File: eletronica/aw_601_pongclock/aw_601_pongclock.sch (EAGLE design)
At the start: 11 parts, among them IC1 MEGA8-P, IC2 4515N, IC3 4515N, IC4 4094N, IC5 4094N, IC6 4094N, IC7 4094N

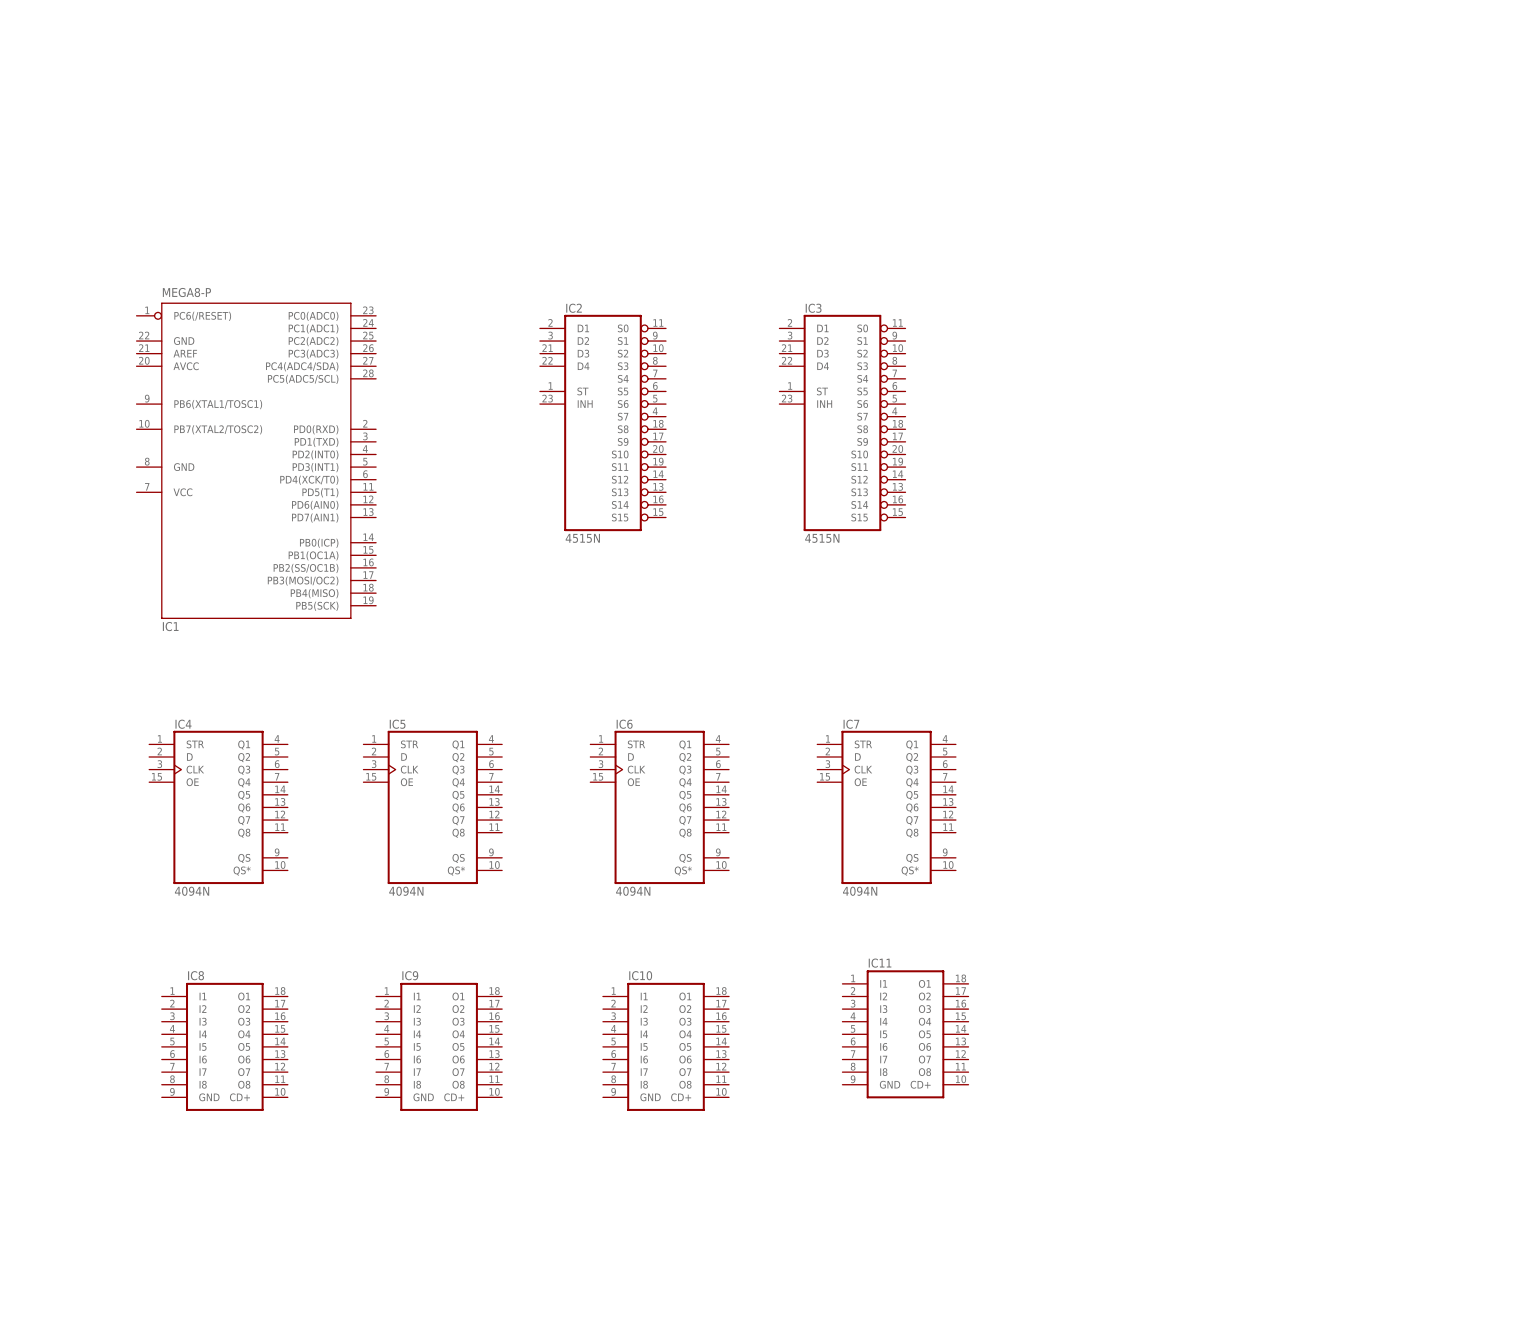
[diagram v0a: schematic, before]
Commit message: 
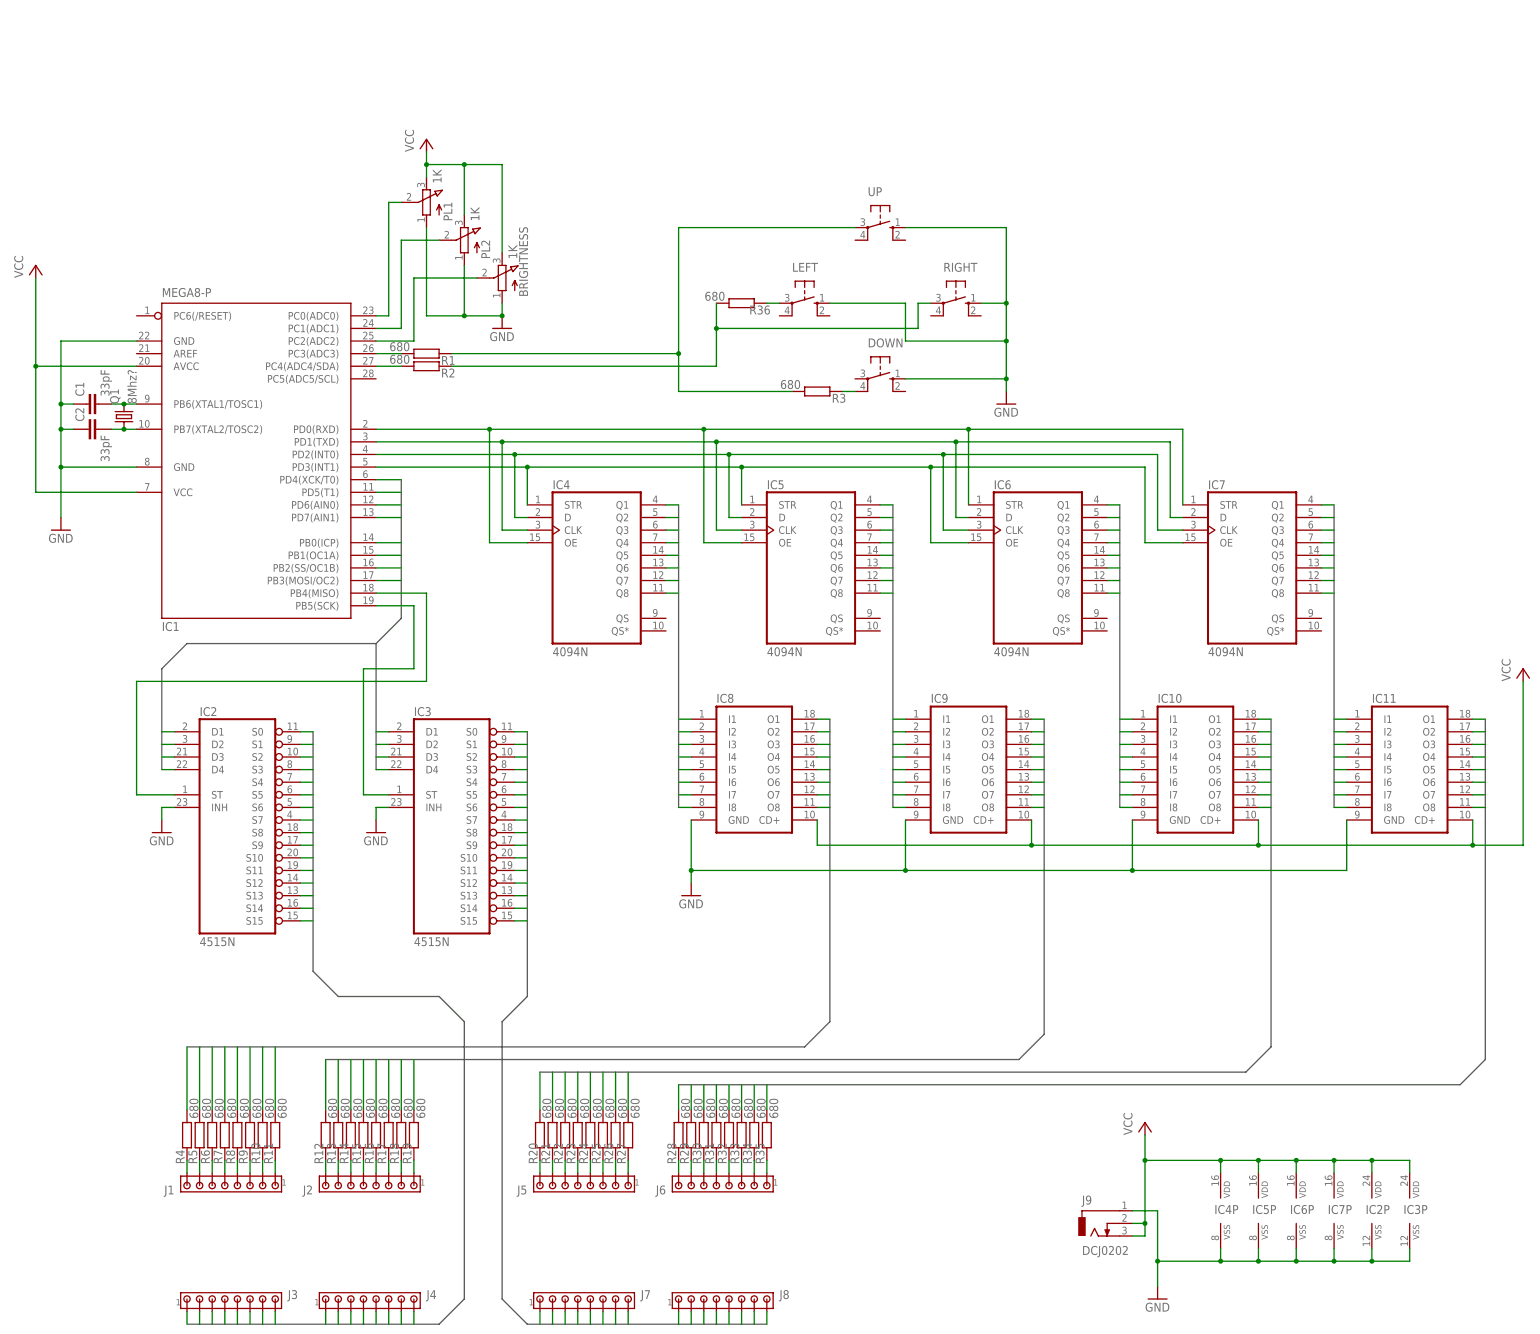
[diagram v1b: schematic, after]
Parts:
- added BRIGHTNESS, PL1, PL2: 1K, pot:3RP/1610N
- added C1, C2: 33pF, rcl:C-EU025-025X050
- added DOWN, LEFT, RIGHT, UP: (no value), switch-omron:40/XX
- added J1, J2, J3, J4, J5, J6, J7, J8: (no value), con-amp:MTA08-100
- added J9: DCJ0202, con-jack:DCJ0202
- added Q1: 8Mhz?, crystal:CRYSTALHC49U70
- added R1, R10, R11, R12, R13, R14, R15, R16, R17, R18, R19, R2, R20, R21, R22, R23, R24, R25, R26, R27, R28, R29, R3, R30, R31, R32, R33, R34, R35, R36, R4, R5, R6, R7, R8, R9: 680, rcl:R-EU_0207/10
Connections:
- new net CATH1_0: IC2A.S0, J3.1
- new net CATH1_1: IC2A.S1, J3.2
- new net CATH1_10: IC2A.S10, J4.3
- new net CATH1_11: IC2A.S11, J4.4
- new net CATH1_12: IC2A.S12, J4.5
- new net CATH1_13: IC2A.S13, J4.6
- new net CATH1_14: IC2A.S14, J4.7
- new net CATH1_15: IC2A.S15, J4.8
- new net CATH1_2: IC2A.S2, J3.3
- new net CATH1_3: IC2A.S3, J3.4
- new net CATH1_4: IC2A.S4, J3.5
- new net CATH1_5: IC2A.S5, J3.6
- new net CATH1_6: IC2A.S6, J3.7
- new net CATH1_7: IC2A.S7, J3.8
- new net CATH1_8: IC2A.S8, J4.1
- new net CATH1_9: IC2A.S9, J4.2
- new net CATH2_0: IC3A.S0, J7.1
- new net CATH2_1: IC3A.S1, J7.2
- new net CATH2_10: IC3A.S10, J8.3
- new net CATH2_11: IC3A.S11, J8.4
- new net CATH2_12: IC3A.S12, J8.5
- new net CATH2_13: IC3A.S13, J8.6
- new net CATH2_14: IC3A.S14, J8.7
- new net CATH2_15: IC3A.S15, J8.8
- new net CATH2_2: IC3A.S2, J7.3
- new net CATH2_3: IC3A.S3, J7.4
- new net CATH2_4: IC3A.S4, J7.5
- new net CATH2_5: IC3A.S5, J7.6
- new net CATH2_6: IC3A.S6, J7.7
- new net CATH2_7: IC3A.S7, J7.8
- new net CATH2_8: IC3A.S8, J8.1
- new net CATH2_9: IC3A.S9, J8.2
- new net GND: BRIGHTNESS.A, C1.1, C2.1, DOWN.S, IC1.GND, IC1.GND@1, IC10.GND, IC11.GND, IC2A.INH, IC2P.VSS, IC3A.INH, IC3P.VSS, IC4P.VSS, IC5P.VSS, IC6P.VSS, IC7P.VSS, IC8.GND, IC9.GND, J9.1, LEFT.S, PL1.A, PL2.A, RIGHT.S, UP.S
- new net LED1A1: IC4A.Q1, IC8.I1
- new net LED1A2: IC4A.Q2, IC8.I2
- new net LED1A3: IC4A.Q3, IC8.I3
- new net LED1A4: IC4A.Q4, IC8.I4
- new net LED1A5: IC4A.Q5, IC8.I5
- new net LED1A6: IC4A.Q6, IC8.I6
- new net LED1A7: IC4A.Q7, IC8.I7
- new net LED1A8: IC4A.Q8, IC8.I8
- new net LED1B1: IC5A.Q1, IC9.I1
- new net LED1B2: IC5A.Q2, IC9.I2
- new net LED1B3: IC5A.Q3, IC9.I3
- new net LED1B4: IC5A.Q4, IC9.I4
- new net LED1B5: IC5A.Q5, IC9.I5
- new net LED1B6: IC5A.Q6, IC9.I6
- new net LED1B7: IC5A.Q7, IC9.I7
- new net LED1B8: IC5A.Q8, IC9.I8
- new net LED2A1: IC10.I1, IC6A.Q1
- new net LED2A2: IC10.I2, IC6A.Q2
- new net LED2A3: IC10.I3, IC6A.Q3
- new net LED2A4: IC10.I4, IC6A.Q4
- new net LED2A5: IC10.I5, IC6A.Q5
- new net LED2A6: IC10.I6, IC6A.Q6
- new net LED2A7: IC10.I7, IC6A.Q7
- new net LED2A8: IC10.I8, IC6A.Q8
- new net LED2B1: IC11.I1, IC7A.Q1
- new net LED2B2: IC11.I2, IC7A.Q2
- new net LED2B3: IC11.I3, IC7A.Q3
- new net LED2B4: IC11.I4, IC7A.Q4
- new net LED2B5: IC11.I5, IC7A.Q5
- new net LED2B6: IC11.I6, IC7A.Q6
- new net LED2B7: IC11.I7, IC7A.Q7
- new net LED2B8: IC11.I8, IC7A.Q8
- new net LEDGND0: IC1.PD4(XCK/T0), IC2A.D1
- new net LEDGND1: IC1.PD5(T1), IC2A.D2
- new net LEDGND2: IC1.PD6(AIN0), IC2A.D3
- new net LEDGND3: IC1.PD7(AIN1), IC2A.D4
- new net LEDGND4: IC1.PB0(ICP), IC3A.D1
- new net LEDGND5: IC1.PB1(OC1A), IC3A.D2
- new net LEDGND6: IC1.PB2(SS/OC1B), IC3A.D3
- new net LEDGND7: IC1.PB3(MOSI/OC2), IC3A.D4
- new net N$1: IC1.PD0(RXD), IC4A.OE, IC5A.OE, IC6A.STR, IC7A.STR
- new net N$10: J1.3, R9.1
- new net N$11: J1.2, R10.1
- new net N$12: J1.1, R11.1
- new net N$13: J2.8, R12.1
- new net N$14: J2.7, R13.1
- new net N$15: J2.6, R14.1
- new net N$16: J2.5, R15.1
- new net N$17: J2.4, R16.1
- new net N$18: J2.3, R17.1
- new net N$19: J2.2, R18.1
- new net N$2: IC1.PD1(TXD), IC4A.CLK, IC5A.CLK, IC6A.D, IC7A.D
- new net N$20: J2.1, R19.1
- new net N$21: J5.8, R20.1
- new net N$22: J5.7, R21.1
- new net N$23: J5.6, R22.1
- new net N$24: J5.5, R23.1
- new net N$25: J5.4, R24.1
- new net N$26: J5.3, R25.1
- new net N$27: J5.2, R26.1
- new net N$28: J5.1, R27.1
- new net N$29: J6.8, R28.1
- new net N$3: IC1.PD2(INT0), IC4A.D, IC5A.D, IC6A.CLK, IC7A.CLK
- new net N$30: J6.7, R29.1
- new net N$31: J6.6, R30.1
- new net N$32: J6.5, R31.1
- new net N$33: J6.4, R32.1
- new net N$34: J6.3, R33.1
- new net N$35: J6.2, R34.1
- new net N$36: J6.1, R35.1
- new net N$37: IC1.PB4(MISO), IC2A.ST
- new net N$38: IC1.PB5(SCK), IC3A.ST
- new net N$39: C1.2, IC1.PB6(XTAL1/TOSC1), Q1.2
- new net N$4: IC1.PD3(INT1), IC4A.STR, IC5A.STR, IC6A.OE, IC7A.OE
- new net N$40: C2.2, IC1.PB7(XTAL2/TOSC2), Q1.1
- new net N$41: IC1.PC0(ADC0), PL1.S
- new net N$42: IC1.PC1(ADC1), PL2.S
- new net N$43: BRIGHTNESS.S, IC1.PC2(ADC2)
- new net N$44: IC1.PC3(ADC3), R1.2
- new net N$45: IC1.PC4(ADC4/SDA), R2.2
- new net N$47: R1.1, R3.2, UP.P
- new net N$48: DOWN.P1, R3.1
- new net N$49: LEFT.P, R36.1
- new net N$5: J1.8, R4.1
- new net N$50: R2.1, R36.2, RIGHT.P
- new net N$6: J1.7, R5.1
- new net N$7: J1.6, R6.1
- new net N$8: J1.5, R7.1
- new net N$9: J1.4, R8.1
- new net TRAN1A1: IC8.O1, R4.2
- new net TRAN1A2: IC8.O2, R5.2
- new net TRAN1A3: IC8.O3, R6.2
- new net TRAN1A4: IC8.O4, R7.2
- new net TRAN1A5: IC8.O5, R8.2
- new net TRAN1A6: IC8.O6, R9.2
- new net TRAN1A7: IC8.O7, R10.2
- new net TRAN1A8: IC8.O8, R11.2
- new net TRAN1B1: IC10.O1, R20.2
- new net TRAN1B2: IC10.O2, R21.2
- new net TRAN1B3: IC10.O3, R22.2
- new net TRAN1B4: IC10.O4, R23.2
- new net TRAN1B5: IC10.O5, R24.2
- new net TRAN1B6: IC10.O6, R25.2
- new net TRAN1B7: IC10.O7, R26.2
- new net TRAN1B8: IC10.O8, R27.2
- new net TRAN2A1: IC9.O1, R12.2
- new net TRAN2A2: IC9.O2, R13.2
- new net TRAN2A3: IC9.O3, R14.2
- new net TRAN2A4: IC9.O4, R15.2
- new net TRAN2A5: IC9.O5, R16.2
- new net TRAN2A6: IC9.O6, R17.2
- new net TRAN2A7: IC9.O7, R18.2
- new net TRAN2A8: IC9.O8, R19.2
- new net TRAN2B1: IC11.O1, R28.2
- new net TRAN2B2: IC11.O2, R29.2
- new net TRAN2B3: IC11.O3, R30.2
- new net TRAN2B4: IC11.O4, R31.2
- new net TRAN2B5: IC11.O5, R32.2
- new net TRAN2B6: IC11.O6, R33.2
- new net TRAN2B7: IC11.O7, R34.2
- new net TRAN2B8: IC11.O8, R35.2
- new net VCC: BRIGHTNESS.E, IC1.AVCC, IC1.VCC@1, IC10.CD+, IC11.CD+, IC2P.VDD, IC3P.VDD, IC4P.VDD, IC5P.VDD, IC6P.VDD, IC7P.VDD, IC8.CD+, IC9.CD+, J9.2, J9.3, PL1.E, PL2.E
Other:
- moved on the sheet: IC10, IC11, IC2, IC3, IC4, IC5, IC6, IC7, IC8, IC9

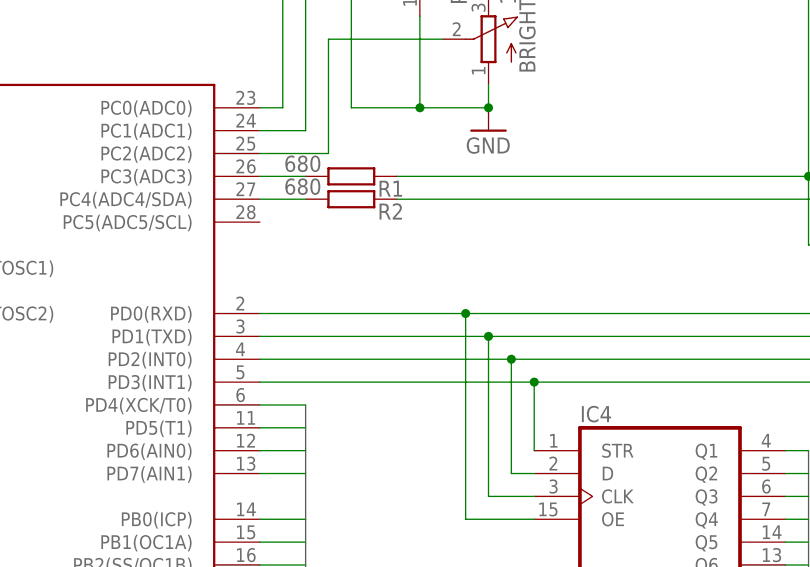
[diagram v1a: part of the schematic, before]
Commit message: 
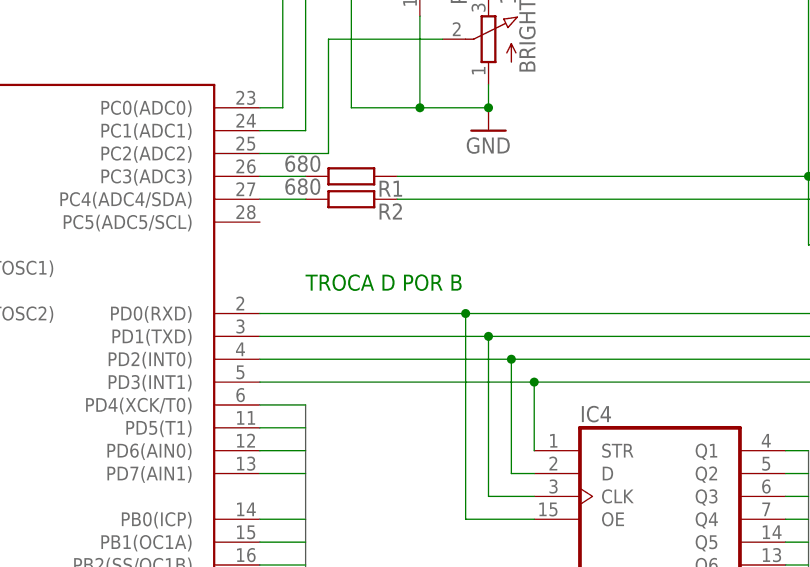
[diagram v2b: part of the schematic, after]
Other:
- note added: "TROCA D POR B"
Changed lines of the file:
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@@
 <grid distance="0.1" unitdist="inch" unit="inch" style="lines" multiple="1" display="no" altdistance="0.01" altunitdist="inch" altunit="inch"/>
 <layers>
-<layer number="1" name="Top" color="4" fill="1" visible="yes" active="no"/>
-<layer number="16" name="Bottom" color="1" fill="1" visible="yes" active="no"/>
-<layer number="17" name="Pads" color="2" fill="1" visible="yes" active="no"/>
-<layer number="18" name="Vias" color="2" fill="1" visible="yes" active="no"/>
-<layer number="19" name="Unrouted" color="6" fill="1" visible="yes" active="no"/>
-<layer number="20" name="Dimension" color="15" fill="1" visible="yes" active="no"/>
-<layer number="21" name="tPlace" color="7" fill="1" visible="yes" active="no"/>
-<layer number="22" name="bPlace" color="7" fill="1" visible="yes" active="no"/>
-<layer number="23" name="tOrigins" color="15" fill="1" visible="yes" active="no"/>
-<layer number="24" name="bOrigins" color="15" fill="1" visible="yes" active="no"/>
-<layer number="25" name="tNames" color="7" fill="1" visible="yes" active="no"/>
-<layer number="26" name="bNames" color="7" fill="1" visible="yes" active="no"/>
-<layer number="27" name="tValues" color="7" fill="1" visible="yes" active="no"/>
-<layer number="28" name="bValues" color="7" fill="1" visible="yes" active="no"/>
+<layer number="1" name="Top" color="4" fill="1" visible="no" active="no"/>
+<layer number="16" name="Bottom" color="1" fill="1" visible="no" active="no"/>
+<layer number="17" name="Pads" color="2" fill="1" visible="no" active="no"/>
+<layer number="18" name="Vias" color="2" fill="1" visible="no" active="no"/>
+<layer number="19" name="Unrouted" color="6" fill="1" visible="no" active="no"/>
+<layer number="20" name="Dimension" color="15" fill="1" visible="no" active="no"/>
+<layer number="21" name="tPlace" color="7" fill="1" visible="no" active="no"/>
+<layer number="22" name="bPlace" color="7" fill="1" visible="no" active="no"/>
+<layer number="23" name="tOrigins" color="15" fill="1" visible="no" active="no"/>
+<layer number="24" name="bOrigins" color="15" fill="1" visible="no" active="no"/>
+<layer number="25" name="tNames" color="7" fill="1" visible="no" active="no"/>
+<layer number="26" name="bNames" color="7" fill="1" visible="no" active="no"/>
+<layer number="27" name="tValues" color="7" fill="1" visible="no" active="no"/>
+<layer number="28" name="bValues" color="7" fill="1" visible="no" active="no"/>
 <layer number="29" name="tStop" color="7" fill="3" visible="no" active="no"/>
 <layer number="30" name="bStop" color="7" fill="6" visible="no" active="no"/>
@@
 <layer number="35" name="tGlue" color="7" fill="4" visible="no" active="no"/>
 <layer number="36" name="bGlue" color="7" fill="5" visible="no" active="no"/>
-<layer number="37" name="tTest" color="7" fill="1" visible="yes" active="no"/>
-<layer number="38" name="bTest" color="7" fill="1" visible="yes" active="no"/>
+<layer number="37" name="tTest" color="7" fill="1" visible="no" active="no"/>
+<layer number="38" name="bTest" color="7" fill="1" visible="no" active="no"/>
 <layer number="39" name="tKeepout" color="4" fill="11" visible="no" active="no"/>
 <layer number="40" name="bKeepout" color="1" fill="11" visible="no" active="no"/>
@@
 <layer number="44" name="Drills" color="7" fill="1" visible="no" active="no"/>
 <layer number="45" name="Holes" color="7" fill="1" visible="no" active="no"/>
-<layer number="46" name="Milling" color="3" fill="1" visible="yes" active="no"/>
-<layer number="47" name="Measures" color="7" fill="1" visible="yes" active="no"/>
-<layer number="48" name="Document" color="7" fill="1" visible="yes" active="no"/>
-<layer number="49" name="Reference" color="7" fill="1" visible="yes" active="no"/>
-<layer number="51" name="tDocu" color="6" fill="9" visible="yes" active="no"/>
-<layer number="52" name="bDocu" color="7" fill="1" visible="yes" active="no"/>
+<layer number="46" name="Milling" color="3" fill="1" visible="no" active="no"/>
+<layer number="47" name="Measures" color="7" fill="1" visible="no" active="no"/>
+<layer number="48" name="Document" color="7" fill="1" visible="no" active="no"/>
+<layer number="49" name="Reference" color="7" fill="1" visible="no" active="no"/>
+<layer number="51" name="tDocu" color="6" fill="9" visible="no" active="no"/>
+<layer number="52" name="bDocu" color="7" fill="1" visible="no" active="no"/>
 <layer number="91" name="Nets" color="2" fill="1" visible="yes" active="yes"/>
 <layer number="92" name="Busses" color="1" fill="1" visible="yes" active="yes"/>
@@
 <sheet>
 <plain>
+<text x="60.96" y="233.68" size="1.778" layer="91">TROCA D POR B</text>
 </plain>
 <instances>
